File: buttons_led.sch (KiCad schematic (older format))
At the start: 26 parts, among them Q1301 2N7002P, SW1301 SW_Push, SW1302 SW_Push, SW1303 SW_Push, SW1304 SW_Push, SW1305 SW_Push, SW1306 SW_Push

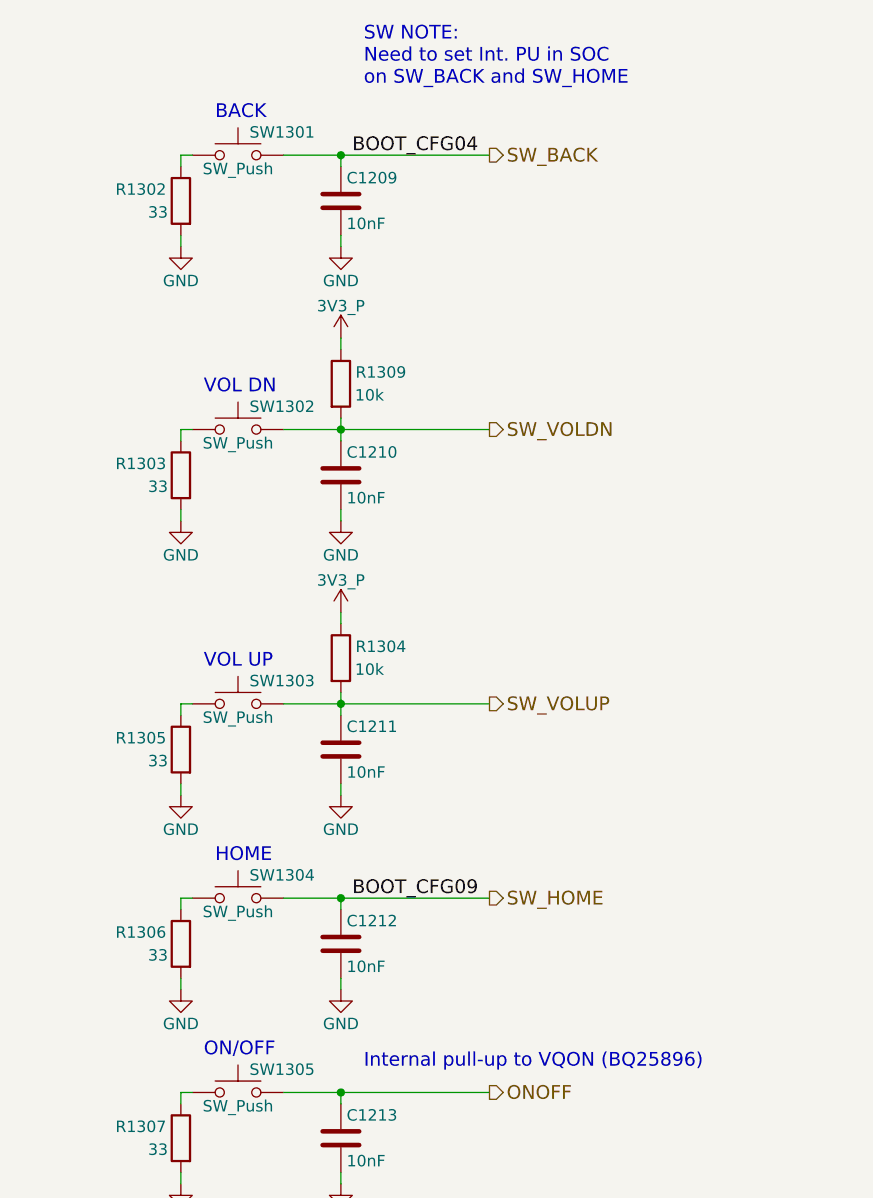
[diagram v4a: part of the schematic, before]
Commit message: Use a DP3T switch to select between eMMC, USB (serial download), and uSD boot devices, corrected the SW_BACK and SW_HOME buttons to have 33Ohm pull-ups instead of pull-downs since the respective boot config lines have pull-downs already set
These buttons should be untouched during boot otherwise the board will not boot properly (pressing SW_HOME during boot causes "SD power cycle enable/eMMC reset enable" and pressing SW_BACK causes the uSD to be treated as a 4-bit bus if it's the boot device otherwise it's a BOOTCONFIG[6:4]=011 "reserved" condition)
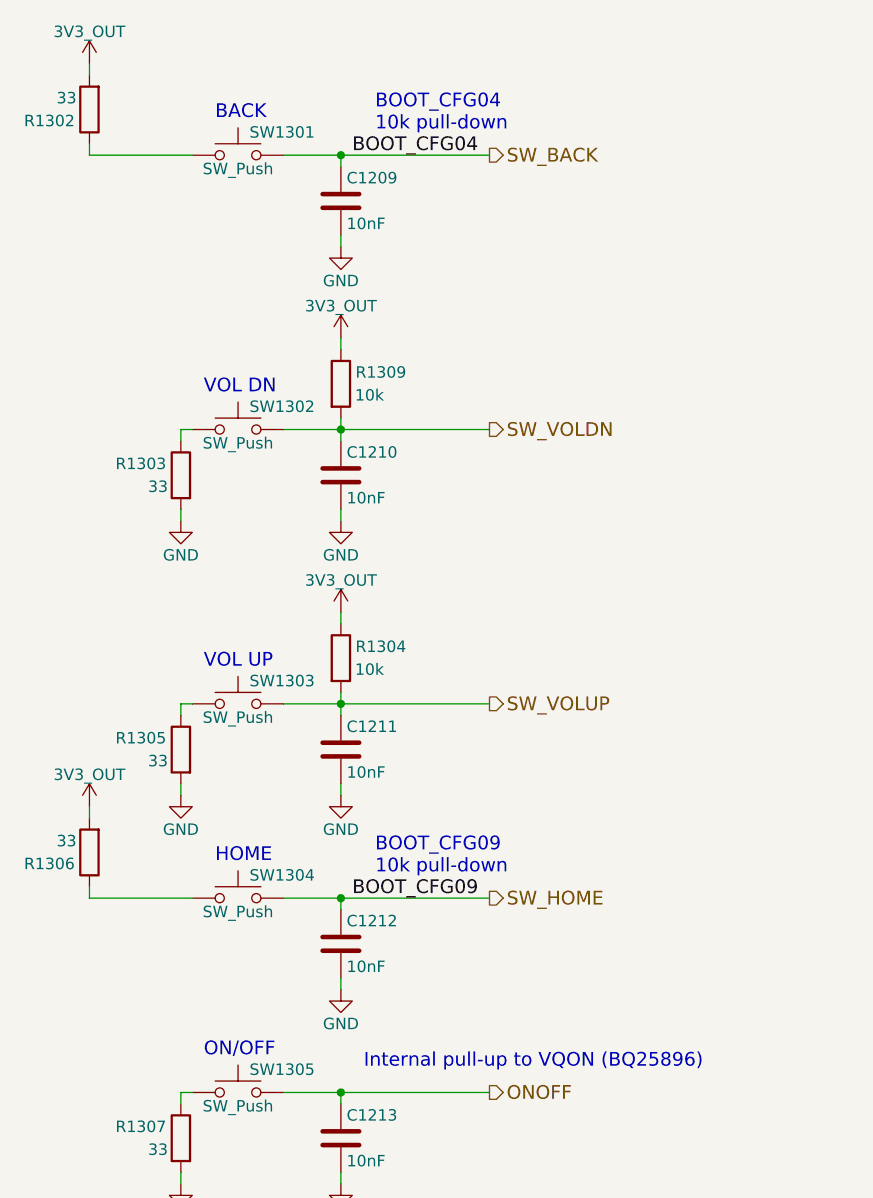
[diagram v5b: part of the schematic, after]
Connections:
- net 3V3_P: no longer R1304.1, R1309.1
- net GND: no longer R1302.2, R1306.2
- new net 3V3_OUT: R1302.2, R1304.1, R1306.2, R1309.1
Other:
- note added: "BOOT_CFG04\n10k pull-down"
- note added: "BOOT_CFG09\n10k pull-down"
- note removed: "SW NOTE:\nNeed to set Int. PU in SOC\non SW_BACK and SW_HOME"
- moved on the sheet: R1302, R1306
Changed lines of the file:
@@
 Sheet 12 21
 Title "Buttons & LED"
-Date "2018-05-15"
+Date "2018-05-16"
 Rev "v0.1.0"
 Comp "Purism SPC"
@@
 $EndComp
 Wire Wire Line
-	2950 1300 2950 1350
-Wire Wire Line
-	2950 1300 3000 1300
+	2550 1300 3000 1300
+Wire Wire Line
+	2950 2500 2950 2550
+Wire Wire Line
+	2950 2500 3000 2500
 $Comp
 L GND #PWR0157
-U 1 1 5ACC4A3B
-P 2950 1700
-F 0 "#PWR0157" H 2950 1450 50  0001 C CNN
-F 1 "GND" H 2950 1550 50  0000 C CNN
-F 2 "" H 2950 1700 50  0001 C CNN
-F 3 "" H 2950 1700 50  0001 C CNN
-	1    2950 1700
-	1    0    0    -1
-$EndComp
-Wire Wire Line
-	2950 2500 2950 2550
-Wire Wire Line
-	2950 2500 3000 2500
-$Comp
-L GND #PWR0158
 U 1 1 5ACC4CAE
 P 2950 2900
-F 0 "#PWR0158" H 2950 2650 50  0001 C CNN
+F 0 "#PWR0157" H 2950 2650 50  0001 C CNN
 F 1 "GND" H 2950 2750 50  0000 C CNN
 F 2 "" H 2950 2900 50  0001 C CNN
@@
 	2950 3700 3000 3700
 $Comp
-L GND #PWR0159
+L GND #PWR0158
 U 1 1 5ACC4CDD
 P 2950 4100
-F 0 "#PWR0159" H 2950 3850 50  0001 C CNN
+F 0 "#PWR0158" H 2950 3850 50  0001 C CNN
 F 1 "GND" H 2950 3950 50  0000 C CNN
 F 2 "" H 2950 4100 50  0001 C CNN
@@
 $EndComp
 Wire Wire Line
-	2950 4550 2950 4600
-Wire Wire Line
-	2950 4550 3000 4550
-$Comp
-L GND #PWR0160
-U 1 1 5ACC4E99
-P 2950 4950
-F 0 "#PWR0160" H 2950 4700 50  0001 C CNN
-F 1 "GND" H 2950 4800 50  0000 C CNN
-F 2 "" H 2950 4950 50  0001 C CNN
-F 3 "" H 2950 4950 50  0001 C CNN
-	1    2950 4950
-	1    0    0    -1
-$EndComp
+	2550 4550 3000 4550
 Wire Wire Line
 	2950 5400 2950 5450
@@
 	2950 5400 3000 5400
 $Comp
-L GND #PWR0161
+L GND #PWR0159
 U 1 1 5ACC4EB3
 P 2950 5800
-F 0 "#PWR0161" H 2950 5550 50  0001 C CNN
+F 0 "#PWR0159" H 2950 5550 50  0001 C CNN
 F 1 "GND" H 2950 5650 50  0000 C CNN
 F 2 "" H 2950 5800 50  0001 C CNN
@@
 $EndComp
 $Comp
-L GND #PWR0162
+L GND #PWR0160
 U 1 1 5ACC7D2C
 P 8750 4000
-F 0 "#PWR0162" H 8750 3750 50  0001 C CNN
+F 0 "#PWR0160" H 8750 3750 50  0001 C CNN
 F 1 "GND" H 8750 3850 50  0000 C CNN
 F 2 "" H 8750 4000 50  0001 C CNN
@@
 LTST-C19HE1WT\n  RBG Option
 $Comp
-L 3V3_P #PWR0163
+L 3V3_P #PWR0161
 U 1 1 5AEA32FD
 P 8750 2800
-F 0 "#PWR0163" H 8750 2650 50  0001 C CNN
+F 0 "#PWR0161" H 8750 2650 50  0001 C CNN
 F 1 "3V3_P" H 8750 2940 50  0000 C CNN
 F 2 "" H 8750 2800 50  0001 C CNN
@@
 	2950 6600 3000 6600
 $Comp
-L GND #PWR0164
+L GND #PWR0162
 U 1 1 5AFE7AC6
 P 2950 7000
-F 0 "#PWR0164" H 2950 6750 50  0001 C CNN
+F 0 "#PWR0162" H 2950 6750 50  0001 C CNN
 F 1 "GND" H 2950 6850 50  0000 C CNN
 F 2 "" H 2950 7000 50  0001 C CNN
@@
 $EndComp
 $Comp
-L 3V3_P #PWR0165
-U 1 1 5B070F70
-P 3650 3300
-F 0 "#PWR0165" H 3650 3150 50  0001 C CNN
-F 1 "3V3_P" H 3650 3440 50  0000 C CNN
-F 2 "" H 3650 3300 50  0001 C CNN
-F 3 "" H 3650 3300 50  0001 C CNN
-	1    3650 3300
-	1    0    0    -1
-$EndComp
-$Comp
 L R R1302
 U 1 1 5B071BF2
-P 2950 1500
-F 0 "R1302" H 3125 1550 50  0000 C CNN
-F 1 "33" H 3050 1450 50  0000 C CNN
-F 2 "" V 2880 1500 50  0001 C CNN
-F 3 "" H 2950 1500 50  0001 C CNN
-	1    2950 1500
-	-1   0    0    -1
+P 2550 1100
+F 0 "R1302" H 2725 1150 50  0000 C CNN
+F 1 "33" H 2650 1050 50  0000 C CNN
+F 2 "" V 2480 1100 50  0001 C CNN
+F 3 "" H 2550 1100 50  0001 C CNN
+	1    2550 1100
+	-1   0    0    1
 $EndComp
 Wire Wire Line
 	2950 7000 2950 6950
 Wire Wire Line
-	2950 1700 2950 1650
+	2550 900  2550 950
 Wire Wire Line
 	2950 2900 2950 2850
@@
 	2950 4100 2950 4050
 Wire Wire Line
-	2950 4950 2950 4900
-Wire Wire Line
 	2950 5800 2950 5750
 Wire Wire Line
 	3400 4550 4300 4550
-$Comp
-L 3V3_P #PWR0166
-U 1 1 5B077FFE
-P 3650 2100
-F 0 "#PWR0166" H 3650 1950 50  0001 C CNN
-F 1 "3V3_P" H 3650 2240 50  0000 C CNN
-F 2 "" H 3650 2100 50  0001 C CNN
-F 3 "" H 3650 2100 50  0001 C CNN
-	1    3650 2100
-	1    0    0    -1
-$EndComp
 $Comp
 L R R1303
@@
 L R R1306
 U 1 1 5B0788EA
-P 2950 4750
-F 0 "R1306" H 3125 4800 50  0000 C CNN
-F 1 "33" H 3050 4700 50  0000 C CNN
-F 2 "" V 2880 4750 50  0001 C CNN
-F 3 "" H 2950 4750 50  0001 C CNN
-	1    2950 4750
-	-1   0    0    -1
+P 2550 4350
+F 0 "R1306" H 2725 4400 50  0000 C CNN
+F 1 "33" H 2650 4300 50  0000 C CNN
+F 2 "" V 2480 4350 50  0001 C CNN
+F 3 "" H 2550 4350 50  0001 C CNN
+	1    2550 4350
+	-1   0    0    1
 $EndComp
 $Comp
@@
 Connection ~ 3650 3700
 Connection ~ 3650 2500
-Text Notes 3750 1000 0    60   ~ 0
-SW NOTE:\nNeed to set Int. PU in SOC\non SW_BACK and SW_HOME
 $Comp
 L R R1310
@@
 $EndComp
 $Comp
-L 3V3_P #PWR0167
+L 3V3_P #PWR0163
 U 1 1 5B16D254
 P 3650 6200
-F 0 "#PWR0167" H 3650 6050 50  0001 C CNN
+F 0 "#PWR0163" H 3650 6050 50  0001 C CNN
 F 1 "3V3_P" H 3650 6340 50  0000 C CNN
 F 2 "" H 3650 6200 50  0001 C CNN
@@
 $EndComp
 $Comp
-L GND #PWR0168
+L GND #PWR0164
 U 1 1 5AF8646F
 P 3650 1700
-F 0 "#PWR0168" H 3650 1450 50  0001 C CNN
+F 0 "#PWR0164" H 3650 1450 50  0001 C CNN
 F 1 "GND" H 3650 1550 50  0000 C CNN
 F 2 "" H 3650 1700 50  0001 C CNN
@@
 $EndComp
 $Comp
-L GND #PWR0169
+L GND #PWR0165
 U 1 1 5AF882B5
 P 3650 2900
-F 0 "#PWR0169" H 3650 2650 50  0001 C CNN
+F 0 "#PWR0165" H 3650 2650 50  0001 C CNN
 F 1 "GND" H 3650 2750 50  0000 C CNN
 F 2 "" H 3650 2900 50  0001 C CNN
@@
 $EndComp
 $Comp
-L GND #PWR0170
+L GND #PWR0166
 U 1 1 5AF899AE
 P 3650 4100
-F 0 "#PWR0170" H 3650 3850 50  0001 C CNN
+F 0 "#PWR0166" H 3650 3850 50  0001 C CNN
 F 1 "GND" H 3650 3950 50  0000 C CNN
 F 2 "" H 3650 4100 50  0001 C CNN
@@
 $EndComp
 $Comp
-L GND #PWR0171
+L GND #PWR0167
 U 1 1 5AF8B0AA
 P 3650 4950
-F 0 "#PWR0171" H 3650 4700 50  0001 C CNN
+F 0 "#PWR0167" H 3650 4700 50  0001 C CNN
 F 1 "GND" H 3650 4800 50  0000 C CNN
 F 2 "" H 3650 4950 50  0001 C CNN
@@
 $EndComp
 $Comp
-L GND #PWR0172
+L GND #PWR0168
 U 1 1 5AF8B58A
 P 3650 5800
-F 0 "#PWR0172" H 3650 5550 50  0001 C CNN
+F 0 "#PWR0168" H 3650 5550 50  0001 C CNN
 F 1 "GND" H 3650 5650 50  0000 C CNN
 F 2 "" H 3650 5800 50  0001 C CNN
@@
 $EndComp
 $Comp
-L GND #PWR0173
+L GND #PWR0169
 U 1 1 5AF8B7F2
 P 3650 7000
-F 0 "#PWR0173" H 3650 6750 50  0001 C CNN
+F 0 "#PWR0169" H 3650 6750 50  0001 C CNN
 F 1 "GND" H 3650 6850 50  0000 C CNN
 F 2 "" H 3650 7000 50  0001 C CNN
@@
 Connection ~ 8050 3750
 $Comp
-L GND #PWR0174
+L GND #PWR0170
 U 1 1 5AFF8032
 P 8050 4150
-F 0 "#PWR0174" H 8050 3900 50  0001 C CNN
+F 0 "#PWR0170" H 8050 3900 50  0001 C CNN
 F 1 "GND" H 8050 4000 50  0000 C CNN
 F 2 "" H 8050 4150 50  0001 C CNN
@@
 Wire Wire Line
 	8050 4150 8050 4100
+$Comp
+L 3V3_OUT #PWR0171
+U 1 1 5B0B843E
+P 3650 2100
+F 0 "#PWR0171" H 3650 1950 50  0001 C CNN
+F 1 "3V3_OUT" H 3650 2240 50  0000 C CNN
+F 2 "" H 3650 2100 50  0001 C CNN
+F 3 "" H 3650 2100 50  0001 C CNN
+	1    3650 2100
+	1    0    0    -1
+$EndComp
+$Comp
+L 3V3_OUT #PWR0172
+U 1 1 5B0BA66C
+P 3650 3300
+F 0 "#PWR0172" H 3650 3150 50  0001 C CNN
+F 1 "3V3_OUT" H 3650 3440 50  0000 C CNN
+F 2 "" H 3650 3300 50  0001 C CNN
+F 3 "" H 3650 3300 50  0001 C CNN
+	1    3650 3300
+	1    0    0    -1
+$EndComp
+$Comp
+L 3V3_OUT #PWR0173
+U 1 1 5B1502EE
+P 2550 4150
+F 0 "#PWR0173" H 2550 4000 50  0001 C CNN
+F 1 "3V3_OUT" H 2550 4290 50  0000 C CNN
+F 2 "" H 2550 4150 50  0001 C CNN
+F 3 "" H 2550 4150 50  0001 C CNN
+	1    2550 4150
+	1    0    0    -1
+$EndComp
+Wire Wire Line
+	2550 4150 2550 4200
+Wire Wire Line
+	2550 4500 2550 4550
+Text Notes 3800 4450 0    60   ~ 0
+BOOT_CFG09\n10k pull-down
+$Comp
+L 3V3_OUT #PWR0174
+U 1 1 5B1B7426
+P 2550 900
+F 0 "#PWR0174" H 2550 750 50  0001 C CNN
+F 1 "3V3_OUT" H 2550 1040 50  0000 C CNN
+F 2 "" H 2550 900 50  0001 C CNN
+F 3 "" H 2550 900 50  0001 C CNN
+	1    2550 900
+	1    0    0    -1
+$EndComp
+Wire Wire Line
+	2550 1250 2550 1300
+Text Notes 3800 1200 0    60   ~ 0
+BOOT_CFG04\n10k pull-down
 $EndSCHEMATC

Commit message: Add current sense resistors and jumper symbols in the schematic, assign the various signals left unspecified, complete the PWR_EN assignment and verify that thepower sequence would be brought up in the correct order, add an LED to the VBAT_REG rail for debugging purposes (know when the board is receiving power)
Both the GP_LED1 and the HAPTIC motor are able to be controlled via PWM2 by individually MUXing the corresponding pads to PWM2. Only one pin should be MUXed to PWM2 at a time whilst the other is a GPIO, otherwise they will behave identically.

The I2C buses do not need the bus switch found on the EmCraft baseboard since the M.2 modules' power is controlled by PWR_EN and their I2C is level shifted between 1.8V<->3.3V, making it safe to leave them as is.

The various sense resistors have their corresponding parts selected but will be "NC" in the BoM and will not be assembled during manufacturing. To measure the current on the various rails (and WLAN M.2), one will need to break the trace between the two pads and place the corresponding resistor. A jumper (1.27 or 2.45 still needs to be determined) can be used to re-short these pads.

Notes have been added regarding which GPIO pins can easily be interchanged if it improves the layout.

Selected a better/cheaper RJ45 receptacle. Also picked out a well-suited green LED to be used in various spots throughout the board.
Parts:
- removed D1306: LED, symbol LED
- added D1201: GREEN_LED, symbol LED_ALT
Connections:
- net at Q1301.3 (D): now also D1201.1 (K)
- net at R1301.2: now also D1201.2 (A)
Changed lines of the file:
@@
 Sheet 12 21
 Title "Buttons & LED"
-Date "2018-05-16"
+Date "2018-05-18"
 Rev "v0.1.0"
 Comp "Purism SPC"
@@
 	2950 2500 3000 2500
 $Comp
-L GND #PWR0176
+L GND #PWR0175
 U 1 1 5ACC4CAE
 P 2950 2900
-F 0 "#PWR0176" H 2950 2650 50  0001 C CNN
+F 0 "#PWR0175" H 2950 2650 50  0001 C CNN
 F 1 "GND" H 2950 2750 50  0000 C CNN
 F 2 "" H 2950 2900 50  0001 C CNN
@@
 	2950 3700 3000 3700
 $Comp
-L GND #PWR0177
+L GND #PWR0176
 U 1 1 5ACC4CDD
 P 2950 4100
-F 0 "#PWR0177" H 2950 3850 50  0001 C CNN
+F 0 "#PWR0176" H 2950 3850 50  0001 C CNN
 F 1 "GND" H 2950 3950 50  0000 C CNN
 F 2 "" H 2950 4100 50  0001 C CNN
@@
 	2950 5400 3000 5400
 $Comp
-L GND #PWR0178
+L GND #PWR0177
 U 1 1 5ACC4EB3
 P 2950 5800
-F 0 "#PWR0178" H 2950 5550 50  0001 C CNN
+F 0 "#PWR0177" H 2950 5550 50  0001 C CNN
 F 1 "GND" H 2950 5650 50  0000 C CNN
 F 2 "" H 2950 5800 50  0001 C CNN
@@
 	3400 5400 4300 5400
 $Comp
-L LED D1306
-U 1 1 5ACC7C6F
-P 8750 3350
-F 0 "D1306" V 8800 3525 50  0000 C CNN
-F 1 "LED" V 8700 3500 50  0000 C CNN
-F 2 "" H 8750 3350 50  0001 C CNN
-F 3 "" H 8750 3350 50  0001 C CNN
-	1    8750 3350
-	0    -1   -1   0
-$EndComp
-$Comp
 L Q_NMOS_GSD Q1301
 U 1 1 5ACC7CF3
@@
 $EndComp
 $Comp
-L GND #PWR0179
+L GND #PWR0178
 U 1 1 5ACC7D2C
 P 8750 4000
-F 0 "#PWR0179" H 8750 3750 50  0001 C CNN
+F 0 "#PWR0178" H 8750 3750 50  0001 C CNN
 F 1 "GND" H 8750 3850 50  0000 C CNN
 F 2 "" H 8750 4000 50  0001 C CNN
@@
 LTST-C19HE1WT\n  RBG Option
 $Comp
-L 3V3_P #PWR0180
+L 3V3_P #PWR0179
 U 1 1 5AEA32FD
 P 8750 2800
-F 0 "#PWR0180" H 8750 2650 50  0001 C CNN
+F 0 "#PWR0179" H 8750 2650 50  0001 C CNN
 F 1 "3V3_P" H 8750 2940 50  0000 C CNN
 F 2 "" H 8750 2800 50  0001 C CNN
@@
 	2950 6600 3000 6600
 $Comp
-L GND #PWR0181
+L GND #PWR0180
 U 1 1 5AFE7AC6
 P 2950 7000
-F 0 "#PWR0181" H 2950 6750 50  0001 C CNN
+F 0 "#PWR0180" H 2950 6750 50  0001 C CNN
 F 1 "GND" H 2950 6850 50  0000 C CNN
 F 2 "" H 2950 7000 50  0001 C CNN
@@
 $EndComp
 $Comp
-L 3V3_P #PWR0182
+L 3V3_P #PWR0181
 U 1 1 5B16D254
 P 3650 6200
-F 0 "#PWR0182" H 3650 6050 50  0001 C CNN
+F 0 "#PWR0181" H 3650 6050 50  0001 C CNN
 F 1 "3V3_P" H 3650 6340 50  0000 C CNN
 F 2 "" H 3650 6200 50  0001 C CNN
@@
 $EndComp
 $Comp
-L GND #PWR0183
+L GND #PWR0182
 U 1 1 5AF8646F
 P 3650 1700
-F 0 "#PWR0183" H 3650 1450 50  0001 C CNN
+F 0 "#PWR0182" H 3650 1450 50  0001 C CNN
 F 1 "GND" H 3650 1550 50  0000 C CNN
 F 2 "" H 3650 1700 50  0001 C CNN
@@
 $EndComp
 $Comp
-L GND #PWR0184
+L GND #PWR0183
 U 1 1 5AF882B5
 P 3650 2900
-F 0 "#PWR0184" H 3650 2650 50  0001 C CNN
+F 0 "#PWR0183" H 3650 2650 50  0001 C CNN
 F 1 "GND" H 3650 2750 50  0000 C CNN
 F 2 "" H 3650 2900 50  0001 C CNN
@@
 $EndComp
 $Comp
-L GND #PWR0185
+L GND #PWR0184
 U 1 1 5AF899AE
 P 3650 4100
-F 0 "#PWR0185" H 3650 3850 50  0001 C CNN
+F 0 "#PWR0184" H 3650 3850 50  0001 C CNN
 F 1 "GND" H 3650 3950 50  0000 C CNN
 F 2 "" H 3650 4100 50  0001 C CNN
@@
 $EndComp
 $Comp
-L GND #PWR0186
+L GND #PWR0185
 U 1 1 5AF8B0AA
 P 3650 4950
-F 0 "#PWR0186" H 3650 4700 50  0001 C CNN
+F 0 "#PWR0185" H 3650 4700 50  0001 C CNN
 F 1 "GND" H 3650 4800 50  0000 C CNN
 F 2 "" H 3650 4950 50  0001 C CNN
@@
 $EndComp
 $Comp
-L GND #PWR0187
+L GND #PWR0186
 U 1 1 5AF8B58A
 P 3650 5800
-F 0 "#PWR0187" H 3650 5550 50  0001 C CNN
+F 0 "#PWR0186" H 3650 5550 50  0001 C CNN
 F 1 "GND" H 3650 5650 50  0000 C CNN
 F 2 "" H 3650 5800 50  0001 C CNN
@@
 $EndComp
 $Comp
-L GND #PWR0188
+L GND #PWR0187
 U 1 1 5AF8B7F2
 P 3650 7000
-F 0 "#PWR0188" H 3650 6750 50  0001 C CNN
+F 0 "#PWR0187" H 3650 6750 50  0001 C CNN
 F 1 "GND" H 3650 6850 50  0000 C CNN
 F 2 "" H 3650 7000 50  0001 C CNN
@@
 Connection ~ 8050 3750
 $Comp
-L GND #PWR0189
+L GND #PWR0188
 U 1 1 5AFF8032
 P 8050 4150
-F 0 "#PWR0189" H 8050 3900 50  0001 C CNN
+F 0 "#PWR0188" H 8050 3900 50  0001 C CNN
 F 1 "GND" H 8050 4000 50  0000 C CNN
 F 2 "" H 8050 4150 50  0001 C CNN
@@
 	8050 4150 8050 4100
 $Comp
-L 3V3_OUT #PWR0190
+L 3V3_OUT #PWR0189
 U 1 1 5B0B843E
 P 3650 2100
-F 0 "#PWR0190" H 3650 1950 50  0001 C CNN
+F 0 "#PWR0189" H 3650 1950 50  0001 C CNN
 F 1 "3V3_OUT" H 3650 2240 50  0000 C CNN
 F 2 "" H 3650 2100 50  0001 C CNN
@@
 $EndComp
 $Comp
-L 3V3_OUT #PWR0191
+L 3V3_OUT #PWR0190
 U 1 1 5B0BA66C
 P 3650 3300
-F 0 "#PWR0191" H 3650 3150 50  0001 C CNN
+F 0 "#PWR0190" H 3650 3150 50  0001 C CNN
 F 1 "3V3_OUT" H 3650 3440 50  0000 C CNN
 F 2 "" H 3650 3300 50  0001 C CNN
@@
 $EndComp
 $Comp
-L 3V3_OUT #PWR0192
+L 3V3_OUT #PWR0191
 U 1 1 5B1502EE
 P 2550 4150
-F 0 "#PWR0192" H 2550 4000 50  0001 C CNN
+F 0 "#PWR0191" H 2550 4000 50  0001 C CNN
 F 1 "3V3_OUT" H 2550 4290 50  0000 C CNN
 F 2 "" H 2550 4150 50  0001 C CNN
@@
 BOOT_CFG09\n10k pull-down
 $Comp
-L 3V3_OUT #PWR0193
+L 3V3_OUT #PWR0192
 U 1 1 5B1B7426
 P 2550 900
-F 0 "#PWR0193" H 2550 750 50  0001 C CNN
+F 0 "#PWR0192" H 2550 750 50  0001 C CNN
 F 1 "3V3_OUT" H 2550 1040 50  0000 C CNN
 F 2 "" H 2550 900 50  0001 C CNN
@@
 Text Notes 3800 1200 0    60   ~ 0
 BOOT_CFG04\n10k pull-down
+$Comp
+L LED_ALT D1201
+U 1 1 5BAA5022
+P 8750 3350
+F 0 "D1201" V 8750 3150 50  0000 C CNN
+F 1 "GREEN_LED" V 8650 3050 50  0000 C CNN
+F 2 "" H 8750 3350 50  0001 C CNN
+F 3 "https://media.digikey.com/pdf/Data%20Sheets/Lite-On%20PDFs/LTST-C171GKT.pdf" H 8750 3350 50  0001 C CNN
+F 4 "Lite-On" V 8750 3350 60  0001 C CNN "MFG Name"
+F 5 "LTST-C171GKT" V 8750 3350 60  0001 C CNN "MFG Part Num"
+F 6 "LTST-C171GKT" V 8750 3350 60  0001 C CNN "Distrib PN"
+F 7 "https://www.arrow.com/en/products/ltst-c171gkt/lite-on-technology" V 8750 3350 60  0001 C CNN "Distrib Link"
+F 8 "-" V 8750 3350 60  0001 C CNN "Tolerance"
+F 9 "https://octopart.com/search?q=LTST-C171GKT&start=0" V 8750 3350 60  0001 C CNN "Others"
+	1    8750 3350
+	0    -1   -1   0
+$EndComp
 $EndSCHEMATC
